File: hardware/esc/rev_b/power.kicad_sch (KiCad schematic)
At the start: 35 parts, among them J701 AUX_BATTERY, J702 FLIGHT_CAN_POWER, U701 LM5164DDA, U702 AP2112K-3.3TRG1, U703 LM5164DDA

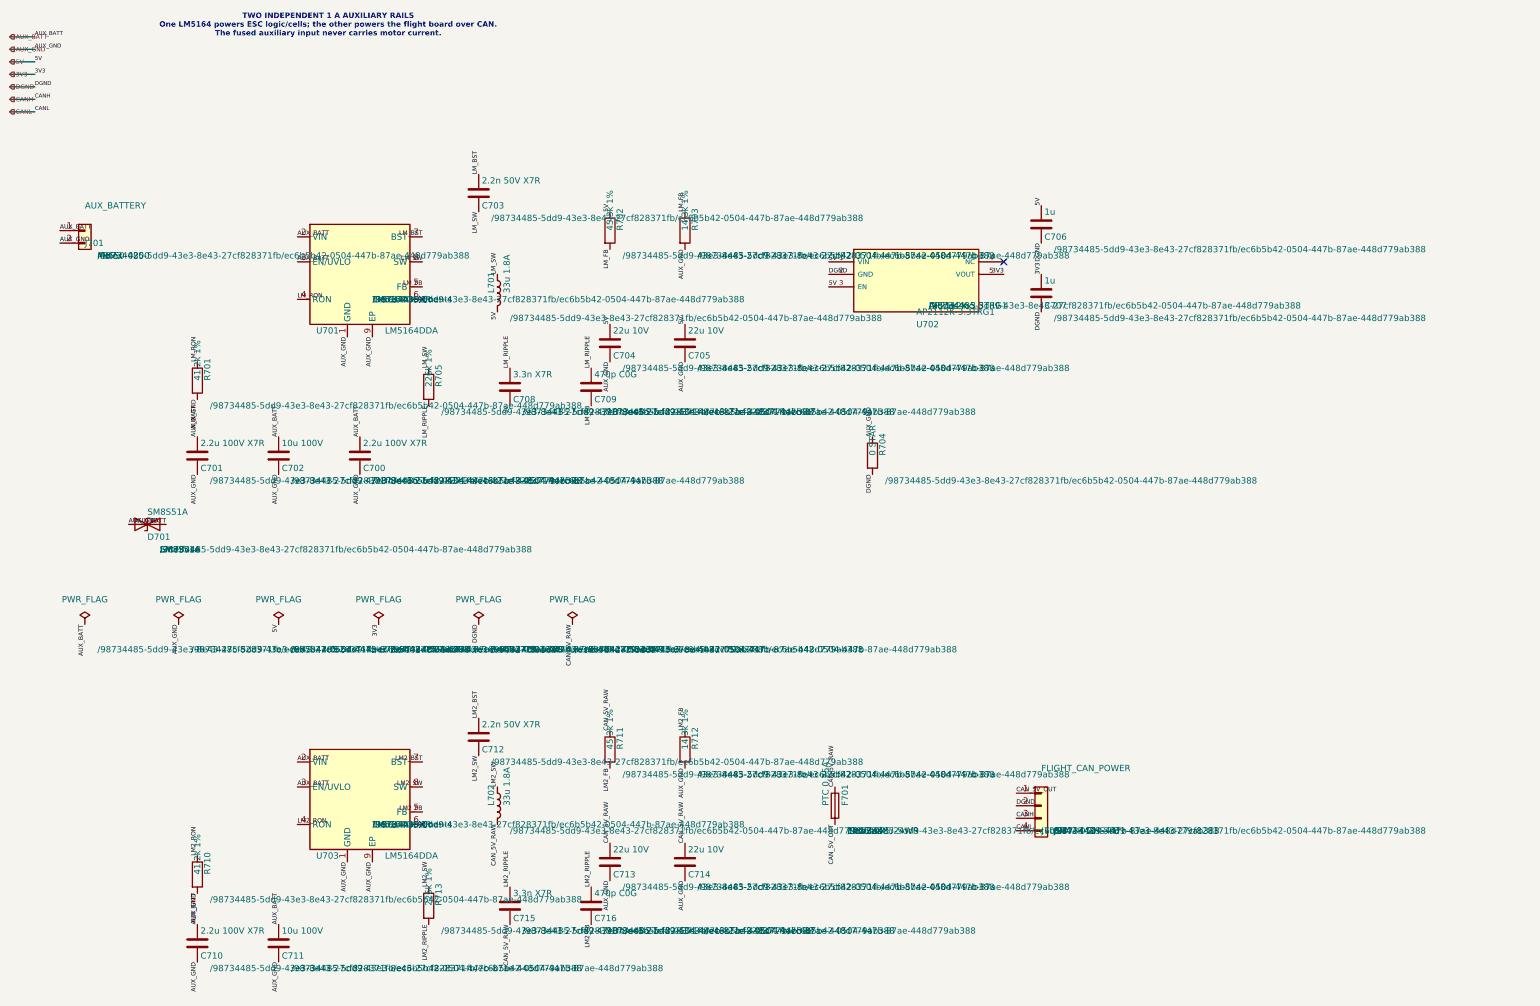
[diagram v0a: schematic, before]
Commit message: Add ESC USB-C programming interfaces
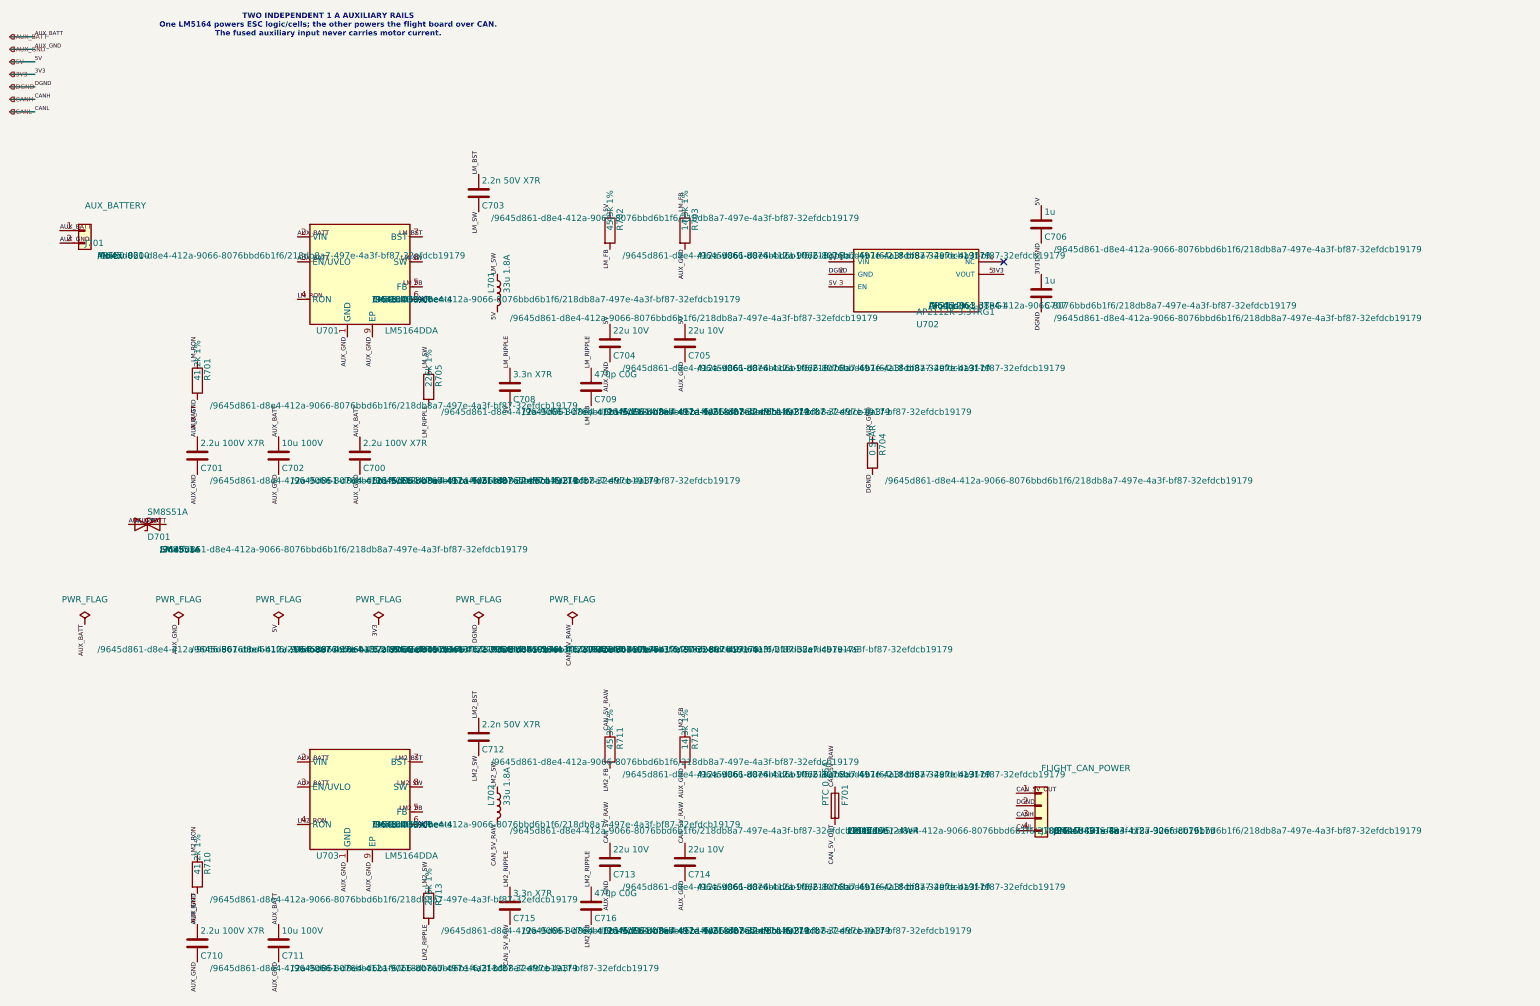
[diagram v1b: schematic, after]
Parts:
- C700, C701, C702, C703, C704, C705, C706, C707, C708, C709, C710, C711, C712, C713, C714, C715, C716, D701, F701, J701, J702, L701, L702, R701, R702, R703, R704, R705, R710, R711, R712, R713, U701, U702, U703: hierarchy_path /98734485-5dd9-43e3-8e43-27cf828371fb/ec6b5b42-0504-447b-87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 -> /9645d861-d8e4-412a-9066-8076bbd6b1f6/218db8a7-497e-4a3f-bf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

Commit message: Keep ESC programming interface to two USB-C ports
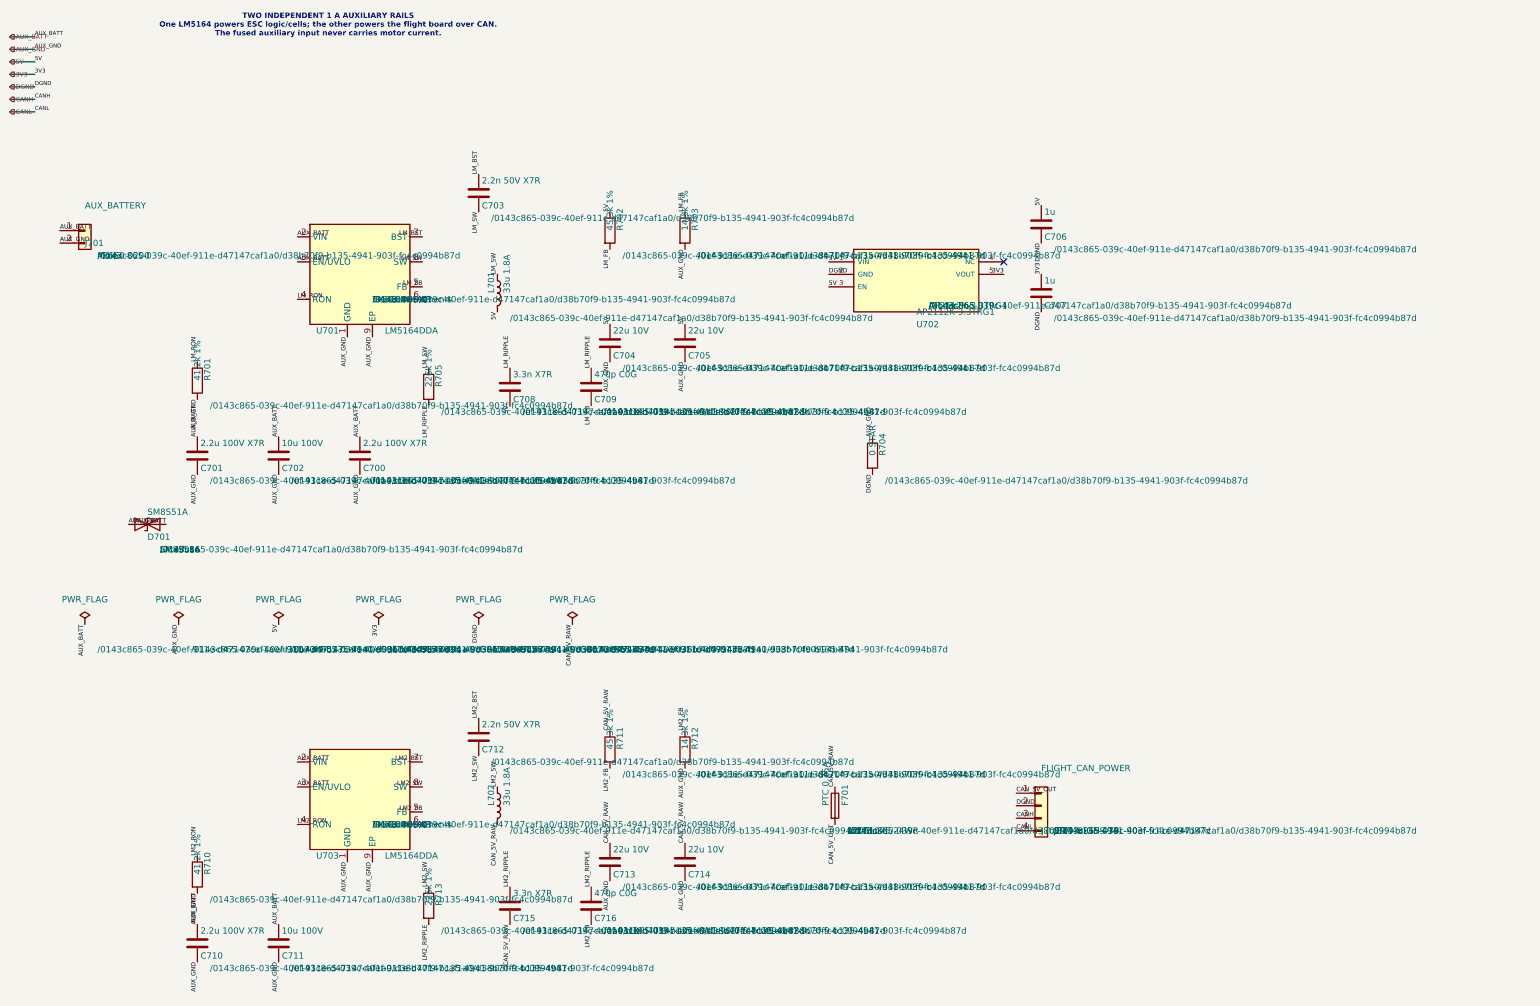
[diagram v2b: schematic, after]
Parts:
- C700, C701, C702, C703, C704, C705, C706, C707, C708, C709, C710, C711, C712, C713, C714, C715, C716, D701, F701, J701, J702, L701, L702, R701, R702, R703, R704, R705, R710, R711, R712, R713, U701, U702, U703: hierarchy_path /9645d861-d8e4-412a-9066-8076bbd6b1f6/218db8a7-497e-4a3f-bf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 -> /0143c865-039c-40ef-911e-d47147caf1a0/d38b70f9-b135-4941-90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

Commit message: Replace ESC selector with seven-pin active-low control
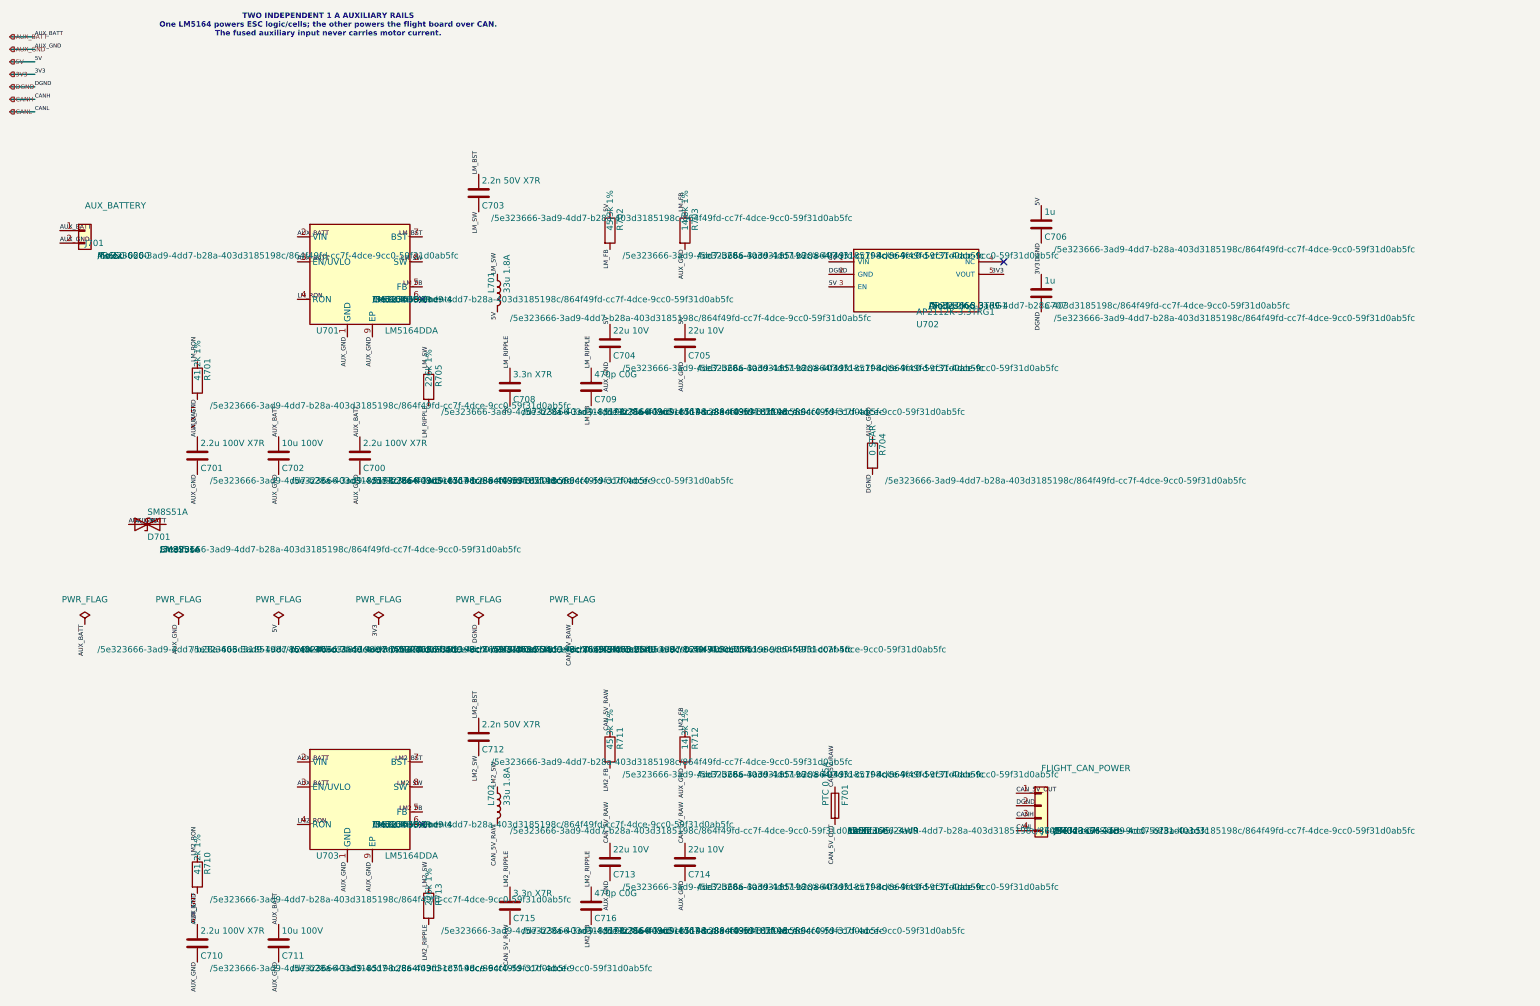
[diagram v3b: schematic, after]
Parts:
- C700, C701, C702, C703, C704, C705, C706, C707, C708, C709, C710, C711, C712, C713, C714, C715, C716, D701, F701, J701, J702, L701, L702, R701, R702, R703, R704, R705, R710, R711, R712, R713, U701, U702, U703: hierarchy_path /0143c865-039c-40ef-911e-d47147caf1a0/d38b70f9-b135-4941-90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 -> /5e323666-3ad9-4dd7-b28a-403d3185198c/864f49fd-cc7f-4dce-9c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
